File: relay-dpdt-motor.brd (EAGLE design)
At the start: 81.3 x 25.1 mm, 9 parts, among them J1 1X2-3.5MM, J2 1X2-3.5MM, K1 4052

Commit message: brd update, wired
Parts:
- moved D1 14.2 mm to (33.0, 11.4), turned to 90 degrees
- moved R2 11.4 mm to (15.2, 11.4), turned to 90 degrees
- moved K1 7.41 mm to (44.5, 7.62)
- moved J2 6.48 mm to (74.9, 7.62), turned to 270 degrees
- moved R1 5.68 mm to (15.2, 2.54)
- moved Q1 5.39 mm to (25.4, 5.08)
- moved Q2 4.58 mm to (27.9, 16.5)
- moved JP1 2.54 mm to (5.08, 5.08)
- moved J1 2.54 mm to (5.08, 16.5)
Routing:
- net +12V: track 0.00 -> 66.1 mm
- net N$5: track 0.00 -> 39.2 mm
- net GND: track 0.00 -> 34.4 mm
- net N$7: track 0.00 -> 23.8 mm
- net N$6: track 0.00 -> 23.8 mm
- net N$2: track 0.00 -> 15.8 mm
- net N$3: track 0.00 -> 13.2 mm
- net N$8: track 0.00 -> 11.2 mm
- net N$1: track 0.00 -> 7.40 mm
- net N$9: track 0.00 -> 6.35 mm
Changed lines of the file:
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@@
 </autorouter>
 <elements>
-<element name="K1" library="relay" package="F4052" value="4052" x="40.64" y="13.97">
-<attribute name="OC_NEWARK" value="unknown" x="40.64" y="13.97" size="1.778" layer="27" display="off"/>
-<attribute name="MPN" value="" x="40.64" y="13.97" size="1.778" layer="27" display="off"/>
-<attribute name="MF" value="" x="40.64" y="13.97" size="1.778" layer="27" display="off"/>
-<attribute name="OC_FARNELL" value="unknown" x="40.64" y="13.97" size="1.778" layer="27" display="off"/>
+<element name="K1" library="relay" package="F4052" value="4052" x="44.45" y="7.62">
+<attribute name="OC_NEWARK" value="unknown" x="44.45" y="7.62" size="1.778" layer="27" display="off"/>
+<attribute name="MPN" value="" x="44.45" y="7.62" size="1.778" layer="27" display="off"/>
+<attribute name="MF" value="" x="44.45" y="7.62" size="1.778" layer="27" display="off"/>
+<attribute name="OC_FARNELL" value="unknown" x="44.45" y="7.62" size="1.778" layer="27" display="off"/>
 </element>
-<element name="Q1" library="dp_devices" package="TO-92" value="" x="29.21" y="8.89" rot="R270"/>
-<element name="Q2" library="adafruit" package="TO220V" value="" x="31.75" y="19.05" rot="R270"/>
-<element name="R1" library="adafruit" package="0204/7" value="" x="17.78" y="7.62"/>
-<element name="D1" library="adafruit" package="DO41-10" value="1N4004" x="45.72" y="5.08" rot="R180"/>
-<element name="J1" library="adafruit" package="1X2-3.5MM" value="1X2-3.5MM" x="5.08" y="19.05" rot="R270"/>
-<element name="R2" library="adafruit" package="0204/7" value="" x="20.32" y="21.59"/>
-<element name="J2" library="adafruit" package="1X2-3.5MM" value="1X2-3.5MM" x="76.2" y="13.97" rot="R90"/>
-<element name="JP1" library="adafruit" package="1X03-CLEANBIG" value="" x="5.08" y="7.62" rot="R270"/>
+<element name="Q1" library="dp_devices" package="TO-92" value="" x="25.4" y="5.08" rot="R270"/>
+<element name="Q2" library="adafruit" package="TO220V" value="" x="27.94" y="16.51" rot="R270"/>
+<element name="R1" library="adafruit" package="0204/7" value="" x="15.24" y="2.54"/>
+<element name="D1" library="adafruit" package="DO41-10" value="1N4004" x="33.02" y="11.43" rot="R90"/>
+<element name="J1" library="adafruit" package="1X2-3.5MM" value="1X2-3.5MM" x="5.08" y="16.51" rot="R270"/>
+<element name="R2" library="adafruit" package="0204/7" value="" x="15.24" y="11.43" rot="R90"/>
+<element name="J2" library="adafruit" package="1X2-3.5MM" value="1X2-3.5MM" x="74.93" y="7.62" rot="R270"/>
+<element name="JP1" library="adafruit" package="1X03-CLEANBIG" value="" x="5.08" y="5.08" rot="R270"/>
 </elements>
 <signals>
@@
 <contactref element="Q1" pad="2"/>
 <contactref element="R1" pad="2"/>
-<wire x1="21.59" y1="7.62" x2="29.21" y2="8.89" width="0" layer="19" extent="1-1"/>
+<wire x1="25.4" y1="5.08" x2="21.59" y2="5.08" width="0.6096" layer="1"/>
+<wire x1="21.59" y1="5.08" x2="19.05" y2="2.54" width="0.6096" layer="1"/>
 </signal>
 <signal name="+12V">
@@
 <contactref element="D1" pad="C"/>
 <contactref element="J1" pad="2"/>
-<wire x1="57.15" y1="10.16" x2="50.8" y2="5.08" width="0" layer="19" extent="1-1"/>
-<wire x1="36.83" y1="17.78" x2="57.15" y2="10.16" width="0" layer="19" extent="1-1"/>
-<wire x1="5.08" y1="20.75" x2="36.83" y2="17.78" width="0" layer="19" extent="1-1"/>
+<wire x1="60.96" y1="3.81" x2="58.42" y2="6.35" width="0.6096" layer="1"/>
+<wire x1="58.42" y1="6.35" x2="48.26" y2="6.35" width="0.6096" layer="1"/>
+<wire x1="48.26" y1="6.35" x2="43.18" y2="11.43" width="0.6096" layer="1"/>
+<wire x1="43.18" y1="11.43" x2="41.91" y2="11.43" width="0.6096" layer="1"/>
+<wire x1="41.91" y1="11.43" x2="40.64" y2="11.43" width="0.6096" layer="1"/>
+<wire x1="33.02" y1="6.35" x2="38.1" y2="11.43" width="0.6096" layer="1"/>
+<wire x1="38.1" y1="11.43" x2="40.64" y2="11.43" width="0.6096" layer="1"/>
+<wire x1="5.08" y1="18.21" x2="7.19" y2="18.21" width="1.016" layer="16"/>
+<wire x1="7.19" y1="18.21" x2="12.7" y2="12.7" width="1.016" layer="16"/>
+<wire x1="12.7" y1="12.7" x2="26.67" y2="12.7" width="1.016" layer="16"/>
+<wire x1="26.67" y1="12.7" x2="33.02" y2="6.35" width="1.016" layer="16"/>
 </signal>
 <signal name="N$2">
 <contactref element="K1" pad="2"/>
 <contactref element="Q1" pad="3"/>
-<wire x1="29.21" y1="6.35" x2="36.83" y2="10.16" width="0" layer="19" extent="1-1"/>
+<wire x1="40.64" y1="3.81" x2="36.83" y2="3.81" width="0.6096" layer="1"/>
+<wire x1="36.83" y1="3.81" x2="35.56" y2="2.54" width="0.6096" layer="1"/>
+<wire x1="35.56" y1="2.54" x2="25.4" y2="2.54" width="0.6096" layer="1"/>
 </signal>
 <signal name="GND">
@@
 <contactref element="Q1" pad="1"/>
 <contactref element="J1" pad="1"/>
-<wire x1="29.21" y1="11.43" x2="29.21" y2="16.51" width="0" layer="19" extent="1-1"/>
-<wire x1="5.08" y1="17.25" x2="29.21" y2="16.51" width="0" layer="19" extent="1-1"/>
-<wire x1="5.08" y1="10.16" x2="5.08" y2="17.25" width="0" layer="19" extent="1-1"/>
+<wire x1="5.08" y1="7.62" x2="5.08" y2="14.71" width="0.6096" layer="1"/>
+<wire x1="5.08" y1="7.62" x2="8.89" y2="7.62" width="0.6096" layer="1"/>
+<wire x1="8.89" y1="7.62" x2="11.43" y2="10.16" width="0.6096" layer="1"/>
+<wire x1="11.43" y1="10.16" x2="22.86" y2="10.16" width="0.6096" layer="1"/>
+<wire x1="22.86" y1="10.16" x2="25.4" y2="7.62" width="0.6096" layer="1"/>
+<wire x1="25.4" y1="13.97" x2="25.4" y2="12.7" width="0.6096" layer="1"/>
+<wire x1="25.4" y1="12.7" x2="22.86" y2="10.16" width="0.6096" layer="1"/>
 </signal>
 <signal name="N$3">
 <contactref element="Q2" pad="1"/>
 <contactref element="R2" pad="2"/>
-<wire x1="24.13" y1="21.59" x2="29.21" y2="21.59" width="0" layer="19" extent="1-1"/>
+<wire x1="15.24" y1="15.24" x2="15.24" y2="17.78" width="0.6096" layer="1"/>
+<wire x1="15.24" y1="17.78" x2="16.51" y2="19.05" width="0.6096" layer="1"/>
+<wire x1="16.51" y1="19.05" x2="25.4" y2="19.05" width="0.6096" layer="1"/>
 </signal>
 <signal name="N$5">
@@
 <contactref element="Q2" pad="2"/>
 <contactref element="D1" pad="A"/>
-<wire x1="40.64" y1="5.08" x2="57.15" y2="17.78" width="0" layer="19" extent="1-1"/>
-<wire x1="29.21" y1="19.05" x2="40.64" y2="5.08" width="0" layer="19" extent="1-1"/>
+<wire x1="60.96" y1="11.43" x2="60.96" y2="13.97" width="0.6096" layer="1"/>
+<wire x1="60.96" y1="13.97" x2="58.42" y2="16.51" width="0.6096" layer="1"/>
+<wire x1="58.42" y1="16.51" x2="33.02" y2="16.51" width="0.6096" layer="1"/>
+<wire x1="33.02" y1="16.51" x2="25.4" y2="16.51" width="0.6096" layer="1"/>
 </signal>
 <signal name="N$6">
@@
 <contactref element="J2" pad="1"/>
 <contactref element="K1" pad="O2"/>
-<wire x1="62.23" y1="10.16" x2="76.2" y2="15.77" width="0" layer="19" extent="1-1"/>
-<wire x1="52.07" y1="17.78" x2="62.23" y2="10.16" width="0" layer="19" extent="1-1"/>
+<wire x1="66.04" y1="3.81" x2="72.92" y2="3.81" width="1.016" layer="1"/>
+<wire x1="72.92" y1="3.81" x2="74.93" y2="5.82" width="0.6096" layer="1"/>
+<wire x1="55.88" y1="11.43" x2="55.88" y2="10.16" width="0.6096" layer="1"/>
+<wire x1="55.88" y1="10.16" x2="58.42" y2="7.62" width="0.6096" layer="1"/>
+<wire x1="58.42" y1="7.62" x2="62.23" y2="7.62" width="0.6096" layer="1"/>
+<wire x1="62.23" y1="7.62" x2="66.04" y2="3.81" width="0.6096" layer="1"/>
 </signal>
 <signal name="N$7">
@@
 <contactref element="K1" pad="S2"/>
 <contactref element="K1" pad="O1"/>
-<wire x1="62.23" y1="17.78" x2="76.2" y2="12.27" width="0" layer="19" extent="1-1"/>
-<wire x1="52.07" y1="10.16" x2="62.23" y2="17.78" width="0" layer="19" extent="1-1"/>
+<wire x1="66.04" y1="11.43" x2="72.82" y2="11.43" width="1.016" layer="1"/>
+<wire x1="72.82" y1="11.43" x2="74.93" y2="9.32" width="1.016" layer="1"/>
+<wire x1="66.04" y1="11.43" x2="62.23" y2="7.62" width="0.6096" layer="16"/>
+<wire x1="62.23" y1="7.62" x2="58.42" y2="7.62" width="0.6096" layer="16"/>
+<wire x1="58.42" y1="7.62" x2="58.42" y2="6.35" width="0.6096" layer="16"/>
+<wire x1="58.42" y1="6.35" x2="55.88" y2="3.81" width="0.6096" layer="16"/>
 </signal>
 <signal name="N$8">
 <contactref element="R2" pad="1"/>
 <contactref element="JP1" pad="2"/>
-<wire x1="5.08" y1="7.62" x2="16.51" y2="21.59" width="0" layer="19" extent="1-1"/>
+<wire x1="5.08" y1="5.08" x2="12.7" y2="5.08" width="0.6096" layer="1"/>
+<wire x1="12.7" y1="5.08" x2="15.24" y2="7.62" width="0.6096" layer="1"/>
 </signal>
 <signal name="N$9">
 <contactref element="R1" pad="1"/>
 <contactref element="JP1" pad="3"/>
-<wire x1="5.08" y1="5.08" x2="13.97" y2="7.62" width="0" layer="19" extent="1-1"/>
+<wire x1="11.43" y1="2.54" x2="5.08" y2="2.54" width="0.6096" layer="1"/>
 </signal>
 </signals>

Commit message: with pnp
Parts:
- removed Q2: (no value), adafruit:TO220V
- added Q3: (no value), dp_devices:TO-92
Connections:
- removed net N$5: D1.A, K1.P2, Q2.2
- new net N$4: D1.C, K1.P1, Q3.1
- net +12V: now also Q3.3; no longer D1.C, K1.P1
- net GND: now also D1.A, K1.P2; no longer Q2.3
- net N$3: now also Q3.2; no longer Q2.1
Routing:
- net +12V: track 66.1 -> 23.9 mm
- net N$5: track 39.2 -> 0.00 mm
- net N$3: track 13.2 -> 4.34 mm
- net GND: track 34.4 -> 33.1 mm
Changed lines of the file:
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@@
 </element>
 <element name="Q1" library="dp_devices" package="TO-92" value="" x="25.4" y="5.08" rot="R270"/>
-<element name="Q2" library="adafruit" package="TO220V" value="" x="27.94" y="16.51" rot="R270"/>
 <element name="R1" library="adafruit" package="0204/7" value="" x="15.24" y="2.54"/>
 <element name="D1" library="adafruit" package="DO41-10" value="1N4004" x="33.02" y="11.43" rot="R90"/>
@@
 <element name="J2" library="adafruit" package="1X2-3.5MM" value="1X2-3.5MM" x="74.93" y="7.62" rot="R270"/>
 <element name="JP1" library="adafruit" package="1X03-CLEANBIG" value="" x="5.08" y="5.08" rot="R270"/>
+<element name="Q3" library="dp_devices" package="TO-92" value="" x="-5.08" y="3.81"/>
 </elements>
 <signals>
@@
 </signal>
 <signal name="+12V">
-<contactref element="K1" pad="1"/>
-<contactref element="K1" pad="P1"/>
-<contactref element="D1" pad="C"/>
 <contactref element="J1" pad="2"/>
-<wire x1="60.96" y1="3.81" x2="58.42" y2="6.35" width="0.6096" layer="1"/>
-<wire x1="58.42" y1="6.35" x2="48.26" y2="6.35" width="0.6096" layer="1"/>
-<wire x1="48.26" y1="6.35" x2="43.18" y2="11.43" width="0.6096" layer="1"/>
-<wire x1="43.18" y1="11.43" x2="41.91" y2="11.43" width="0.6096" layer="1"/>
-<wire x1="41.91" y1="11.43" x2="40.64" y2="11.43" width="0.6096" layer="1"/>
-<wire x1="33.02" y1="6.35" x2="38.1" y2="11.43" width="0.6096" layer="1"/>
-<wire x1="38.1" y1="11.43" x2="40.64" y2="11.43" width="0.6096" layer="1"/>
 <wire x1="5.08" y1="18.21" x2="7.19" y2="18.21" width="1.016" layer="16"/>
 <wire x1="7.19" y1="18.21" x2="12.7" y2="12.7" width="1.016" layer="16"/>
 <wire x1="12.7" y1="12.7" x2="26.67" y2="12.7" width="1.016" layer="16"/>
-<wire x1="26.67" y1="12.7" x2="33.02" y2="6.35" width="1.016" layer="16"/>
+<contactref element="K1" pad="1"/>
+<contactref element="Q3" pad="3"/>
+<wire x1="26.67" y1="12.7" x2="40.64" y2="11.43" width="0" layer="19" extent="16-16"/>
+<wire x1="-2.54" y1="3.81" x2="5.08" y2="18.21" width="0" layer="19" extent="1-1"/>
 </signal>
 <signal name="N$2">
@@
 </signal>
 <signal name="GND">
-<contactref element="Q2" pad="3"/>
 <contactref element="JP1" pad="1"/>
 <contactref element="Q1" pad="1"/>
@@
 <wire x1="11.43" y1="10.16" x2="22.86" y2="10.16" width="0.6096" layer="1"/>
 <wire x1="22.86" y1="10.16" x2="25.4" y2="7.62" width="0.6096" layer="1"/>
-<wire x1="25.4" y1="13.97" x2="25.4" y2="12.7" width="0.6096" layer="1"/>
 <wire x1="25.4" y1="12.7" x2="22.86" y2="10.16" width="0.6096" layer="1"/>
+<contactref element="D1" pad="A"/>
+<contactref element="K1" pad="P2"/>
+<wire x1="33.02" y1="16.51" x2="60.96" y2="11.43" width="0" layer="19" extent="1-1"/>
+<wire x1="25.4" y1="12.7" x2="33.02" y2="16.51" width="0" layer="19" extent="1-1"/>
 </signal>
 <signal name="N$3">
-<contactref element="Q2" pad="1"/>
 <contactref element="R2" pad="2"/>
 <wire x1="15.24" y1="15.24" x2="15.24" y2="17.78" width="0.6096" layer="1"/>
 <wire x1="15.24" y1="17.78" x2="16.51" y2="19.05" width="0.6096" layer="1"/>
-<wire x1="16.51" y1="19.05" x2="25.4" y2="19.05" width="0.6096" layer="1"/>
-</signal>
-<signal name="N$5">
-<contactref element="K1" pad="P2"/>
-<contactref element="Q2" pad="2"/>
-<contactref element="D1" pad="A"/>
-<wire x1="60.96" y1="11.43" x2="60.96" y2="13.97" width="0.6096" layer="1"/>
-<wire x1="60.96" y1="13.97" x2="58.42" y2="16.51" width="0.6096" layer="1"/>
-<wire x1="58.42" y1="16.51" x2="33.02" y2="16.51" width="0.6096" layer="1"/>
-<wire x1="33.02" y1="16.51" x2="25.4" y2="16.51" width="0.6096" layer="1"/>
+<contactref element="Q3" pad="2"/>
+<wire x1="-5.08" y1="3.81" x2="15.24" y2="15.24" width="0" layer="19" extent="1-1"/>
 </signal>
 <signal name="N$6">
@@
 <wire x1="11.43" y1="2.54" x2="5.08" y2="2.54" width="0.6096" layer="1"/>
 </signal>
+<signal name="N$4">
+<contactref element="D1" pad="C"/>
+<contactref element="K1" pad="P1"/>
+<contactref element="Q3" pad="1"/>
+<wire x1="33.02" y1="6.35" x2="60.96" y2="3.81" width="0" layer="19" extent="1-1"/>
+<wire x1="-7.62" y1="3.81" x2="33.02" y2="6.35" width="0" layer="19" extent="1-1"/>
+</signal>
 </signals>

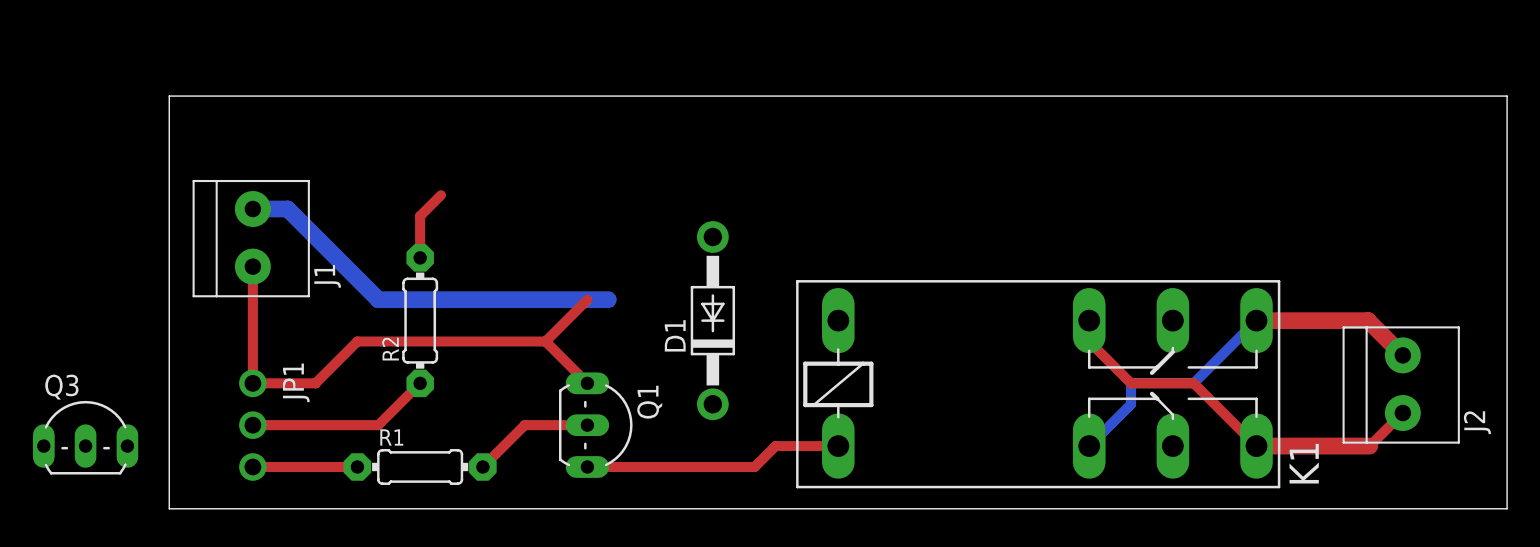
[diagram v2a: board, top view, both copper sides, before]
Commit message: 2 relays one cup, including flyback
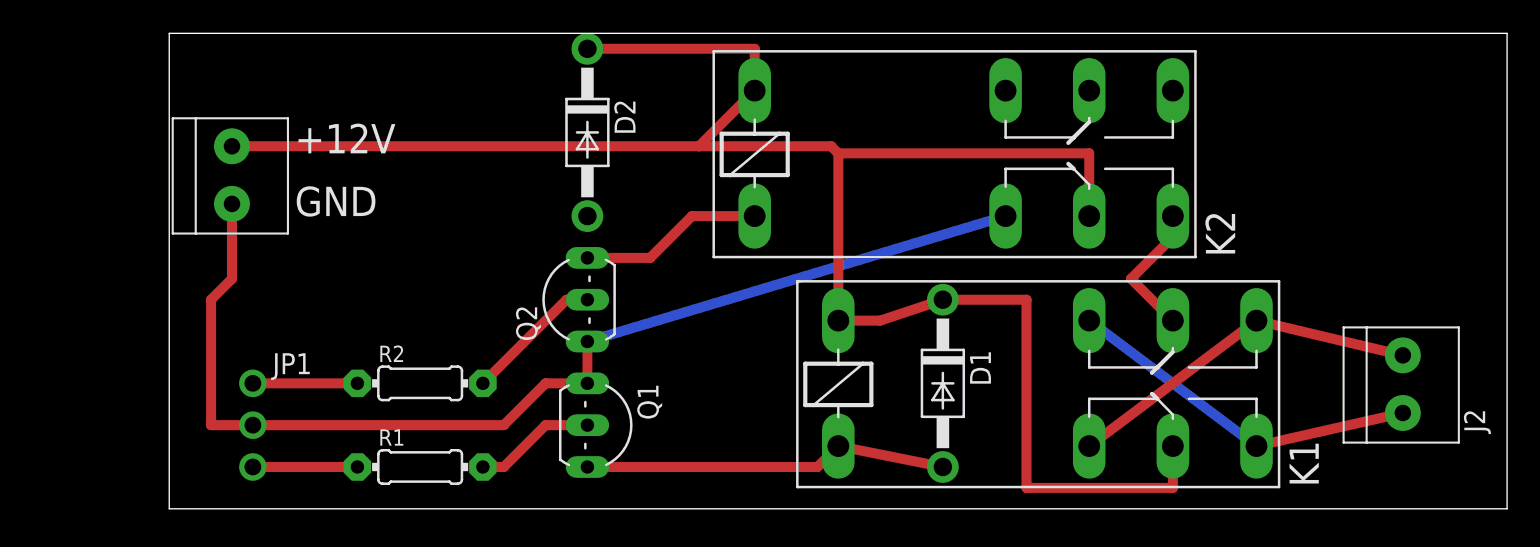
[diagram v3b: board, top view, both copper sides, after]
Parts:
- removed Q3: (no value), dp_devices:TO-92
- added D2: 1N4004, adafruit:DO41-10
- added K2: 4052, relay:F4052
- added Q2: (no value), dp_devices:TO-92
- moved D1 14.5 mm to (47.0, 7.62), turned to 270 degrees
- moved J1 4.02 mm to (3.81, 20.3)
- moved R2 3.81 mm to (15.2, 7.62), turned to 0 degrees
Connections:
- removed net N$4: D1.C, K1.P1, Q3.1
- new net N$10: K1.P2, K2.S1
- new net N$5: JP1.1, R2.1
- net +12V: now also D1.C, D2.C, K1.P1, K2.1, K2.P1; no longer Q3.3
- net GND: now also JP1.2, K2.O1, Q2.1; no longer D1.A, JP1.1, K1.P2
- net N$2: now also D1.A
- net N$3: now also Q2.2; no longer Q3.2
- net N$8: now also D2.A, K2.2, Q2.3; no longer JP1.2, R2.1
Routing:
- net +12V: track 23.9 -> 118.2 mm
- net GND: track 33.1 -> 66.9 mm
- net N$10: track 0.00 -> 8.45 mm
- net N$2: track 15.8 -> 22.2 mm
- net N$5: track 0.00 -> 6.35 mm
- net N$3: track 4.34 -> 8.45 mm
- net N$7: track 23.8 -> 21.8 mm
- net N$6: track 23.8 -> 21.8 mm
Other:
- board size 81.3 x 25.1 mm -> 81.3 x 28.9 mm
- board text added: "+12V"
- board text added: "GND"
